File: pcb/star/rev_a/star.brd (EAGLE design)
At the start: 61.4 x 100 mm, 3 parts

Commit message: got a shape
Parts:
- added A4: FRACTUS-2.4GHZ-FR05-S1-N-0-102, chips:FRACTUS-ANTENNA-FR05-S1-N-0-102
- added B1: BAL-NRF01D3, chips:BAL-NRF01D3
- added C1: 0.8pF, passives:0402_CAP
- added C10: 47nF, passives:0402_CAP
- added C11, C15, C4: 0.1uF, passives:0402_CAP
- added C13, C18: 1uF, passives:0402_CAP
- added C14: 4.7uF, passives:0402_CAP
- added C17: 0.47uF, passives:0402_CAP
- added C2, C3: 12pF, passives:0402_CAP
- added C6: 1nF, passives:0402_CAP
- added C7: 100nF, passives:0402_CAP
- added C8: 2.2nF, passives:0402_CAP
- added J1: MICRO_USB_B_HIROSE_ZX62R-B-5P, connector:USB_MICRO_B-HIROSE-ZX62R-B-5P
- added J2: TC2030-JLINK-NL, connector:TC2030-IDC-NL
- added L1: 15nH, passives:0402_CAP
- added L3: 10uH, passives:0603_CAP
- added LOGO1: UMICH_SOLID_SMALL, logos:UMICH_SOLID_75MIL
- added R10: 25.5k, passives:0402_RES
- added R12: 1M, passives:0402_RES
- added R13: 2M, passives:0402_RES
- added R14: 2.2M, passives:0402_RES
- added R15: 10M, passives:0402_RES
- added R6: 12k, passives:0402_RES
- added U$1, U$2: BAT_FLAT_PAD, connector:BATTERY_FLAT_PAD
- added U2: LTC4065, chips:DFN-6/2MM
- added U4: TPS715AXX, chips:WDFN-6
- added U5: NRF51822QF, chips:QFN-48-6MM
- added X1: EPSON-FA-128, crystals:FA-128
- moved A3 37.5 mm to (10.6, 17.1)
- moved A2 37.3 mm to (36.8, 17.1)
- moved A1 33.9 mm to (23.7, 39.8)
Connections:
- new net !CHRG: R12.1, R13.2, U2.2
- new net !FRAM_CS: U5.21
- new net !FRAM_HOLD: U5.20
- new net !FRAM_WP: U5.22
- new net !RTC_INT: U5.44
- new net AIN3: U5.6
- new net AIN4: U5.7
- new net AIN5: U5.8
- new net AIN6: U5.9
- new net AIN7: U5.10
- new net ANTENNA: A4.1, B1.SE, C1.1
- new net AVDD: C13.1, C6.1, L1.1, U5.35, U5.36
- new net BATIN: C15.2, R14.2, R15.1
- new net BOOTLOADER_CTRL: U5.19
- new net BOOTLOADER_RX: U5.17
- new net BOOTLOADER_TX: U5.18
- new net DCC: L3.2, U5.2
- new net GND: B1.GND, C1.2, C10.2, C11.2, C13.2, C14.2, C15.1, C17.2, C18.2, C2.2, C3.2, C4.2, C6.2, C7.2, C8.2, J1.5, J2.5, R10.1, R13.1, R14.1, R6.1, U$1.M, U$2.M, U2.1, U2.5, U2.7, U4.2, U4.3, U4.4, U4.5, U4.TP, U4.TP2, U4.TP3, U5.13, U5.33, U5.34, U5.GND, X1.2, X1.4
- new net I2C_SCL: U5.5
- new net I2C_SDA: U5.11
- new net LED_BLUE: U5.27
- new net LED_GREEN: U5.28
- new net LED_RED: U5.26
- new net N$10: C2.1, U5.38, X1.3
- new net N$13: R10.2, U2.6
- new net N$15: C10.1, U5.29
- new net N$17: C7.1, U5.39
- new net N$18: B1.ANT1, U5.31
- new net N$19: B1.ANT2, U5.32
- new net N$20: B1.VCC, C8.1, U5.30
- new net N$37: L1.2, L3.1
- new net N$9: C3.1, U5.37, X1.1
- new net P08: U5.14
- new net P09: U5.15
- new net P10: U5.16
- new net P17: U5.25
- new net P21: U5.40
- new net P22: U5.41
- new net P23: U5.42
- new net P24: U5.43
- new net RTC_CE: U5.47
- new net SPI_MISO: U5.48
- new net SPI_MOSI: U5.3
- new net SPI_SCK: U5.4
- new net SWDCLK: J2.4, R6.2, U5.24
- new net SWDIO/!RESET: J2.2, U5.23
- new net VBAT: C4.1, R15.2, U$1.P, U$2.P, U2.3, U4.1
- new net VCC: C11.1, C14.1, C17.1, J2.1, U4.6, U5.1, U5.12
- new net VUSB: C18.1, J1.1, R12.2, U2.4
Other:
- board size 61.4 x 100 mm -> 44.5 x 50.9 mm

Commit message: new shape
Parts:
- added R1, R2: 10k, passives:0402_RES
- moved R6 36.8 mm to (11.7, 6.10)
- moved C13 10.7 mm to (32.4, -1.32), turned to 270 degrees
- moved L1 8.93 mm to (31.4, -1.32), turned to 270 degrees
- moved L3 6.44 mm to (30.2, -0.18), turned to 90 degrees
- moved C14 4.27 mm to (28.6, 1.19), turned to 270 degrees
- moved C7 3.93 mm to (28.0, 7.39)
- moved C11 3.73 mm to (33.3, -1.32)
- moved C2 3.65 mm to (28.5, 8.31)
- moved X1 3.65 mm to (29.4, 9.78)
- moved C3 3.65 mm to (30.3, 11.4)
- moved C6 3.61 mm to (32.7, 9.09), turned to 60 degrees
- moved J1 3.33 mm to (23.7, -2.44)
- moved C8 3.28 mm to (35.9, 7.14)
- moved B1 3.28 mm to (34.6, 8.20)
- moved U5 3.28 mm to (32.7, 3.99)
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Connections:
- net !RTC_INT renamed DW_INT
- removed net !FRAM_CS: U5.21
- removed net !FRAM_HOLD: U5.20
- removed net !FRAM_WP: U5.22
- removed net AIN3: U5.6
- removed net AIN4: U5.7
- removed net AIN5: U5.8
- removed net AIN6: U5.9
- removed net AIN7: U5.10
- removed net BOOTLOADER_CTRL: U5.19
- removed net BOOTLOADER_RX: U5.17
- removed net BOOTLOADER_TX: U5.18
- removed net LED_BLUE: U5.27
- removed net LED_GREEN: U5.28
- removed net LED_RED: U5.26
- removed net P08: U5.14
- removed net P09: U5.15
- removed net P10: U5.16
- removed net P17: U5.25
- removed net P21: U5.40
- removed net P22: U5.41
- removed net P23: U5.42
- removed net P24: U5.43
- removed net RTC_CE: U5.47
- removed net SPI_MISO: U5.48
- removed net SPI_MOSI: U5.3
- removed net SPI_SCK: U5.4
- net I2C_SCL: now also R2.1, U5.47; no longer U5.5
- net I2C_SDA: now also R1.1, U5.48; no longer U5.11
- net VCC: now also R1.2, R2.2
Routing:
- net AVDD: track 0.00 -> 14.2 mm, vias 0 -> 2
- net VUSB: track 0.00 -> 6.29 mm
- net N$10: track 0.00 -> 4.84 mm
- net N$9: track 0.00 -> 4.18 mm
- net SWDIO/!RESET: track 0.00 -> 3.08 mm, vias 0 -> 1
- net N$15: track 0.00 -> 3.03 mm
- net N$20: track 0.00 -> 2.88 mm
- net N$17: track 0.00 -> 2.65 mm
- net VCC: track 0.00 -> 2.28 mm
- net DCC: track 0.00 -> 2.17 mm
- net SWDCLK: track 0.00 -> 2.03 mm, vias 0 -> 1
- net N$37: track 0.00 -> 1.59 mm
- net ANTENNA: track 0.00 -> 1.28 mm
- net N$19: track 0.00 -> 1.08 mm
- net N$18: track 0.00 -> 1.08 mm
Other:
- board size 44.5 x 50.9 mm -> 47 x 49.5 mm

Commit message: more routing
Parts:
- removed R13: 2M, passives:0402_RES
- added D1, D2: (no value), SparkFun-LED:LED-0603
- added R3: 1k, passives:0402_RES
- R10: value 25.5k -> 2k 1%
- R12: value 1M -> 1k
- moved R6 36.5 mm to (31.8, 36.6), turned to 15 degrees
- moved LOGO1 35.9 mm to (27.1, 57.3), turned to 345 degrees
- moved U$1 35.5 mm to (35.6, 63.4), turned to 345 degrees
- moved A1 33.7 mm to (47.0, 64.2), turned to 345 degrees
- moved A3 33.7 mm to (28.5, 45.7), turned to 105 degrees
- moved J2 32.1 mm to (31.0, 39.4), turned to 195 degrees
- moved R14 31.7 mm to (31.1, 34.7), turned to 105 degrees
- moved R10 31.0 mm to (30.2, 30.3), turned to 195 degrees
- moved U$2 31.0 mm to (55.7, 57.8), turned to 345 degrees
- moved C4 30.8 mm to (26.6, 33.6), turned to 105 degrees
- moved C15 30.7 mm to (32.2, 34.9), turned to 105 degrees
- moved R12 30.5 mm to (29.0, 27.5), turned to 165 degrees
- moved U2 30.4 mm to (27.8, 30.7), turned to 195 degrees
- moved C14 30.2 mm to (41.0, 28.7), turned to 75 degrees
- moved R15 30.2 mm to (30.0, 34.5), turned to 285 degrees
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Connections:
- new net !CHRG1: D2.A, R3.1
- new net N$5: D1.C, U2.2
- new net N$6: D2.C, U5.43
- net !CHRG: now also D1.A; no longer R13.2, U2.2
- net GND: no longer R13.1
- net VCC: now also R3.2
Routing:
- net SWDCLK: track 2.03 -> 33.6 mm, vias 1 -> 2
- net VCC: track 2.28 -> 33.7 mm, vias 0 -> 4
- net SWDIO/!RESET: track 3.08 -> 32.8 mm, vias 1 -> 2
- net GND: track 0.00 -> 16.0 mm, vias 16 -> 27
- net N$5: track 0.00 -> 9.19 mm, vias 0 -> 2
- net VUSB: track 6.29 -> 15.4 mm
- net VBAT: track 0.00 -> 7.30 mm
- net N$6: track 0.00 -> 5.06 mm
- net BATIN: track 0.00 -> 2.29 mm
- net !CHRG: track 0.00 -> 1.35 mm
- net N$13: track 0.00 -> 1.26 mm
- net DCC: track 2.17 -> 3.22 mm
- net AVDD: track 14.2 -> 14.7 mm
- added copper zone on layer 1, net GND
- added copper zone on layer 16, net GND
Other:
- board size 47 x 49.5 mm -> 45.4 x 52.6 mm

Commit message: update board
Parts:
- moved LOGO1 33.6 mm to (5.15, 31.9), turned to 0 degrees
- moved U$1 33.4 mm to (11.8, 40.0), turned to 0 degrees
- moved A1 31.9 mm to (22.5, 43.8), turned to 0 degrees
- moved A3 31.1 mm to (9.41, 21.1), turned to 120 degrees
- moved J2 29.5 mm to (13.5, 15.6), turned to 210 degrees
- moved C4 29.4 mm to (10.7, 8.85), turned to 120 degrees
- moved U$2 29.3 mm to (32.6, 39.8), turned to 0 degrees
- moved R6 28.9 mm to (15.0, 13.1), turned to 30 degrees
- moved R15 28.8 mm to (13.8, 10.6), turned to 300 degrees
- moved R14 28.7 mm to (14.8, 11.1), turned to 120 degrees
- moved U2 28.6 mm to (12.7, 6.37), turned to 210 degrees
- moved C15 28.5 mm to (15.8, 11.6), turned to 120 degrees
- moved C18 28.4 mm to (12.8, 4.20), turned to 210 degrees
- moved U4 28.2 mm to (15.8, 8.84), turned to 300 degrees
- moved R10 28.1 mm to (15.0, 6.62), turned to 210 degrees
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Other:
- board size 45.4 x 52.6 mm -> 47 x 49.5 mm

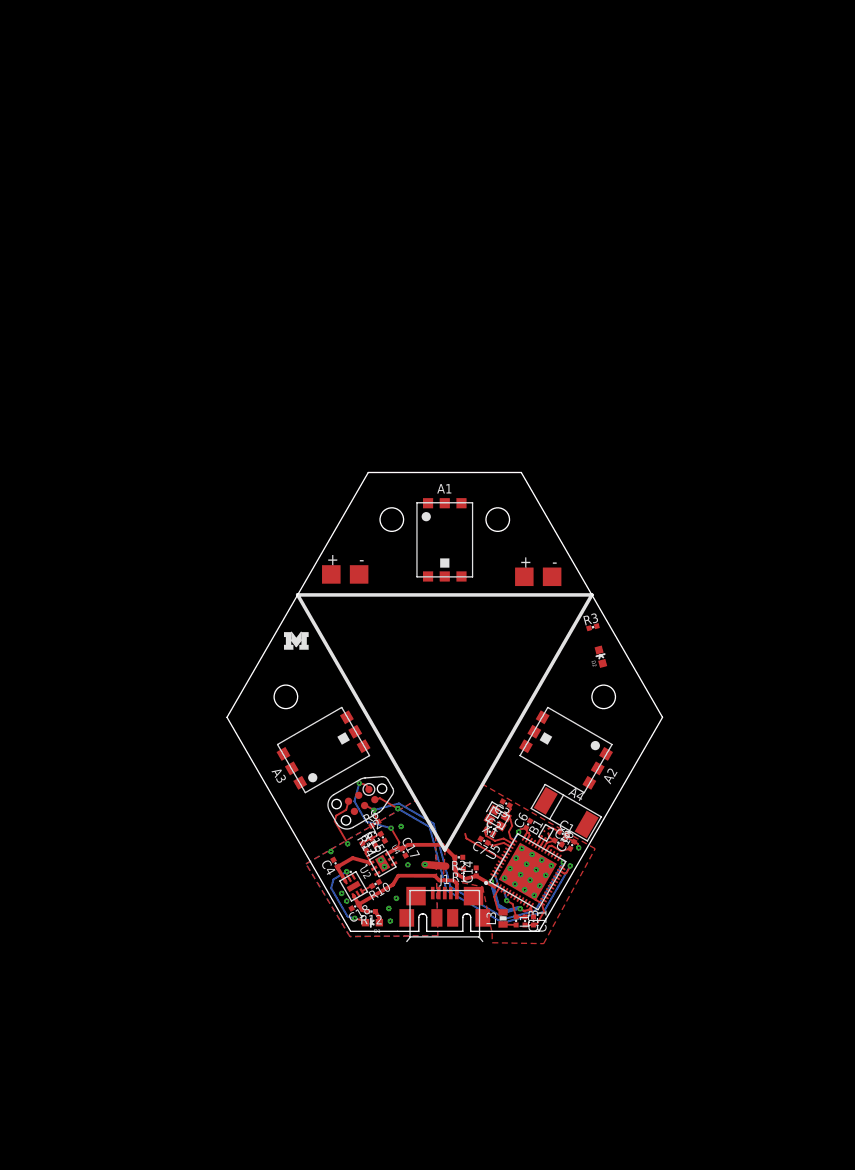
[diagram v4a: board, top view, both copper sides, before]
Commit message: updating pcb
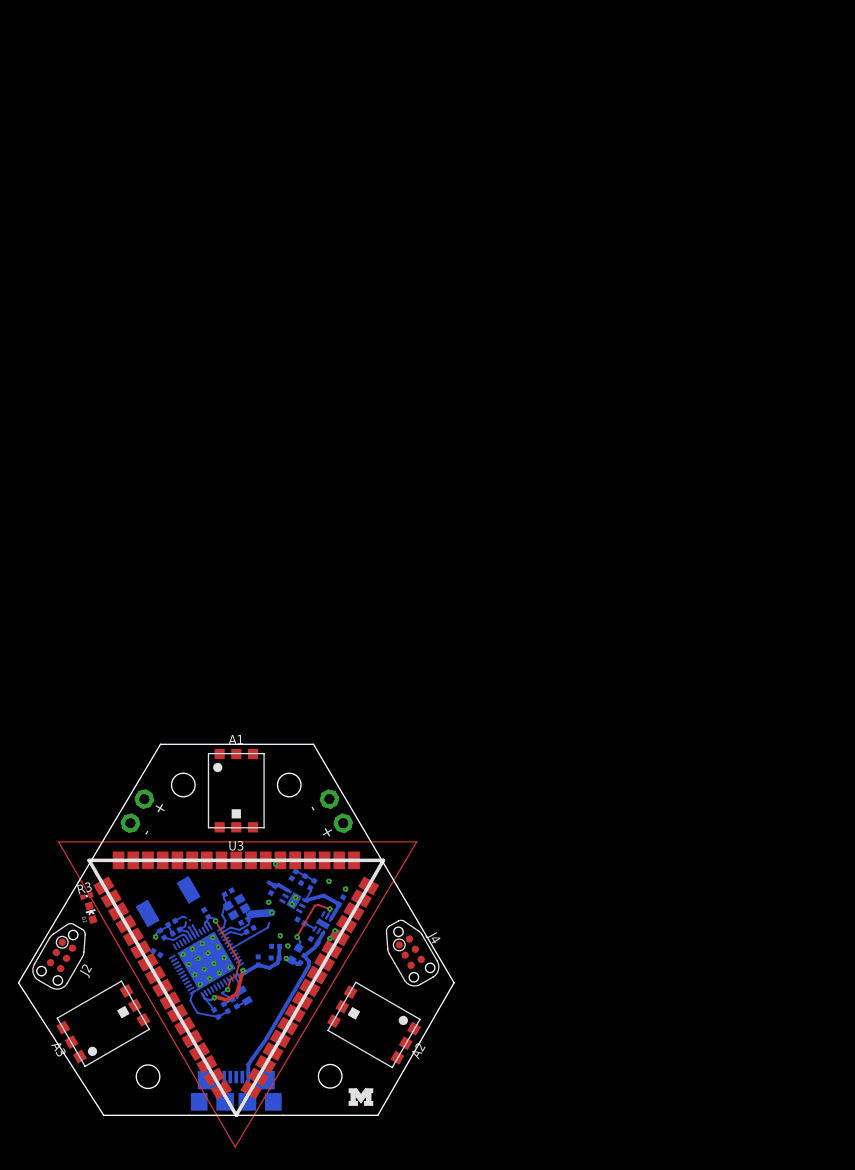
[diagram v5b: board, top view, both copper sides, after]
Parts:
- removed J1: MICRO_USB_B_HIROSE_ZX62R-B-5P, connector:USB_MICRO_B-HIROSE-ZX62R-B-5P
- removed U$1, U$2: BAT_FLAT_PAD, connector:BATTERY_FLAT_PAD
- added J3: MICRO_USB_B_HIROSE_ZX62-B-5PA(11), connector:USB_MICRO_B-HIROSE-ZX62-B-5PA(11)
- added J4: TC2030-JLINK-NL, connector:TC2030-IDC-NL
- added U$3, U$4: BAT_HOLE, connector:BATTERY_HOLE
- added U3: TRIPOINT, tripoint:TRIPOINT
- moved R3 61.9 mm to (-16.1, 5.31)
- moved D2 61.6 mm to (-15.7, 3.52)
- moved LOGO1 49.7 mm to (12.1, -17.3)
- moved C10 45.3 mm to (-7.99, 1.21), flipped to the bottom
- moved A4 44.0 mm to (-7.35, 4.71), flipped to the bottom
- moved C1 43.3 mm to (-6.97, 2.42), flipped to the bottom
- moved C8 42.3 mm to (-6.49, 1.49), flipped to the bottom
- moved B1 39.8 mm to (-5.17, 2.53), flipped to the bottom
- moved A3 37.9 mm to (-14.4, -8.46)
- moved J2 36.5 mm to (-18.9, -1.08), turned to 240 degrees
- moved A2 36.2 mm to (14.9, -8.58)
- moved C6 36.0 mm to (-3.24, 3.44), flipped to the bottom
- moved U5 36.0 mm to (-3.21, -1.66), flipped to the bottom
- moved C11 35.7 mm to (-2.17, -7.35), flipped to the bottom, turned to 240 degrees
- moved A1 35.2 mm to (0.00, 16.7)
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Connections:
- net GND: now also J3.5, J4.5, U$3.N, U$4.N; no longer J1.5, U$1.M, U$2.M
- net VBAT: now also U$3.P, U$4.P; no longer U$1.P, U$2.P
- net VCC: now also J4.1
- net VUSB: now also J3.1; no longer J1.1
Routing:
- net GND: track 16.0 -> 127.6 mm
- net SWDCLK: track 33.6 -> 0.00 mm, vias 2 -> 0
- net SWDIO/!RESET: track 32.8 -> 0.00 mm, vias 2 -> 0
- net VCC: track 34.1 -> 18.3 mm, vias 4 -> 2
- net VUSB: track 15.4 -> 18.3 mm
- net N$5: track 9.19 -> 7.84 mm
- removed copper zone on layer 1, net GND
- removed copper zone on layer 16, net GND
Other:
- board size 47 x 49.5 mm -> 47 x 40 mm

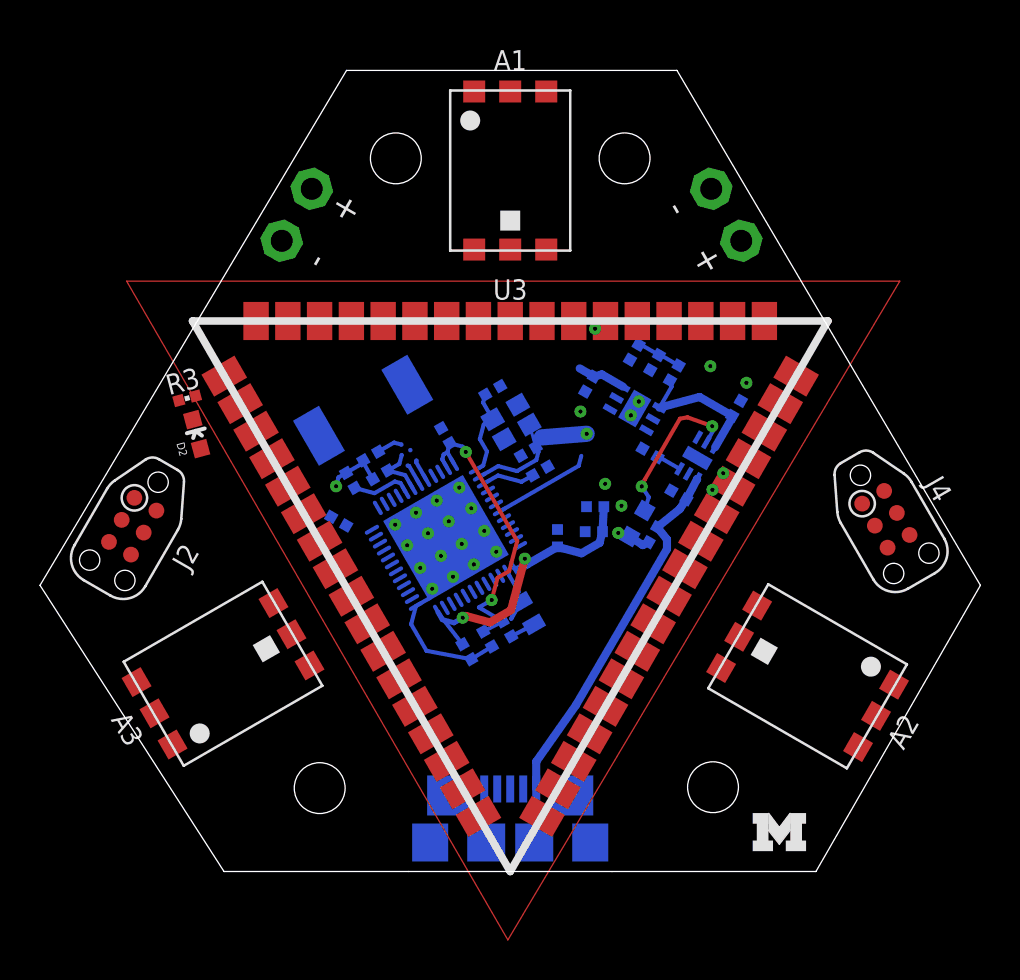
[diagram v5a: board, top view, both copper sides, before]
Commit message: moved led
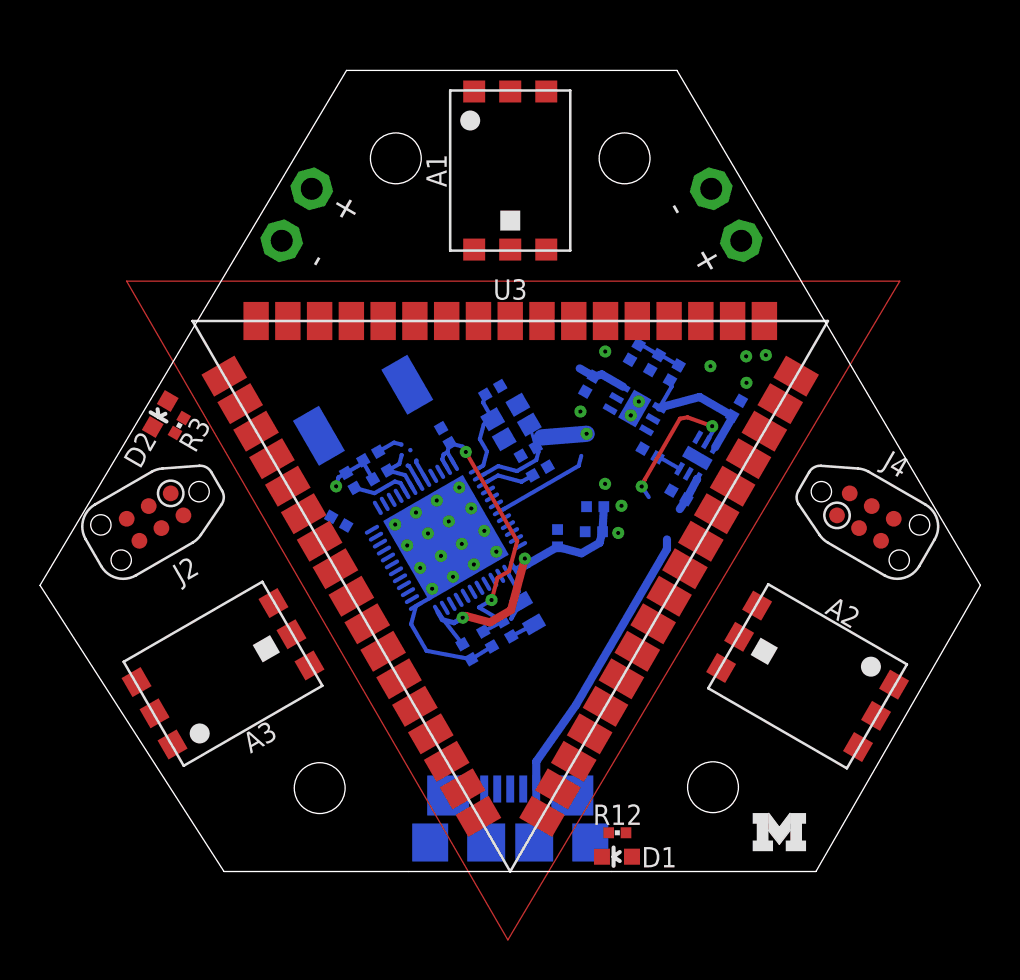
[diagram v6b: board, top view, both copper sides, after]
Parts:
- moved D1 16.7 mm to (5.34, -17.6), flipped to the top, turned to 90 degrees
- moved R12 15.0 mm to (5.35, -16.4), flipped to the top, turned to 180 degrees
- moved D2 2.08 mm to (-17.5, 4.53), turned to 150 degrees
- moved R3 1.42 mm to (-16.5, 3.95), turned to 240 degrees
- moved J2 1.21 mm to (-17.7, -0.63), turned to 210 degrees
- moved J4 1.03 mm to (17.7, -0.63), turned to 330 degrees
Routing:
- net VUSB: track 18.3 -> 16.1 mm
- net !CHRG: track 1.11 -> 0.00 mm
- net N$5: track 7.84 -> 7.15 mm
